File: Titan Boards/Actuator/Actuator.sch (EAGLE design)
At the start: 74 parts, among them Q1 MOSFET-NCH-AO3404A, Q12 MOSFET-NCH-AO3404A, Q13 MOSFET-NCH-AO3404A, Q14 MOSFET-NCH-AO3404A, Q15 MOSFET-NCH-AO3404A, Q17 MOSFET-NCH-AO3404A, Q18 FDD4141TO252, Q2 MOSFET-NCH-AO3404A, Q3 MOSFET-NCH-AO3404A, Q4 MOSFET-NCH-AO3404A, Q5 MOSFET-NCH-AO3404A, Q6 FDD4141TO252, Y1 12MHz, Y3 32.768kHz

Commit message: actuator board work TL
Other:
- note added: "WIP Notes: (I used my board as a start template because it had most of the microcontroller routing) - Moved capacitor to top right - Spaced out the torpedo parts a little - Made the microcontroller a bit more in center -TL 11/12: Routed bottom-left; dropper resistors Things still needed: - Labels positioned for LED's - Cleanup of all labels"
- note removed: "WIP Notes: (I used my board as a start template because it had most of the microcontroller routing) - Moved capacitor to top right - Spaced out the torpedo parts a little - Made the microcontroller a bit more in center Things still needed: - Labels positioned for LED's - Converter section (bottom left) (This is probably something good to take from your board) - Cleanup of all labels"
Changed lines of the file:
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@@
 - Spaced out the torpedo parts a little
 - Made the microcontroller a bit more in center
+-TL 11/12: Routed bottom-left; dropper resistors
 Things still needed:
 - Labels positioned for LED's
-- Converter section (bottom left)
-(This is probably something good to take
-from your board)
 - Cleanup of all labels</text>
 </plain>

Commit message: Titan Actuator Review Copy
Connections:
- net +3V3: now also U$1.SPARE7
- net EXTRA4: no longer U$1.SPARE7
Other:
- note removed: "WIP Notes: (I used my board as a start template because it had most of the microcontroller routing) - Moved capacitor to top right - Spaced out the torpedo parts a little - Made the microcontroller a bit more in center -TL 11/12: Routed bottom-left; dropper resistors Things still needed: - Labels positioned for LED's - Cleanup of all labels"
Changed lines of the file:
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@@
 <part name="AGND15" library="supply1" library_urn="urn:adsk.eagle:library:371" deviceset="AGND" device=""/>
 <part name="FRAME2" library="frames" library_urn="urn:adsk.eagle:library:229" deviceset="A3L-LOC" device=""/>
+<part name="+3V4" library="supply1" library_urn="urn:adsk.eagle:library:371" deviceset="+3V3" device=""/>
+<part name="+3V5" library="supply1" library_urn="urn:adsk.eagle:library:371" deviceset="+3V3" device=""/>
+<part name="+3V6" library="supply1" library_urn="urn:adsk.eagle:library:371" deviceset="+3V3" device=""/>
 </parts>
 <sheets>
@@
 <attribute name="VALUE" x="317.5" y="33.02" size="1.778" layer="96" rot="R180"/>
 </instance>
+<instance part="+3V4" gate="G$1" x="134.62" y="228.6" smashed="yes">
+<attribute name="VALUE" x="137.16" y="231.14" size="1.778" layer="96" rot="R180"/>
+</instance>
+<instance part="+3V5" gate="G$1" x="45.72" y="292.1" smashed="yes">
+<attribute name="VALUE" x="48.26" y="294.64" size="1.778" layer="96" rot="R180"/>
+</instance>
+<instance part="+3V6" gate="G$1" x="119.38" y="17.78" smashed="yes" rot="R180">
+<attribute name="VALUE" x="116.84" y="15.24" size="1.778" layer="96" rot="R90"/>
+</instance>
 </instances>
 <busses>
@@
 </segment>
 <segment>
-<wire x1="134.62" y1="231.14" x2="134.62" y2="210.82" width="0.1524" layer="91"/>
+<wire x1="134.62" y1="231.14" x2="134.62" y2="226.06" width="0.1524" layer="91"/>
+<wire x1="134.62" y1="226.06" x2="134.62" y2="210.82" width="0.1524" layer="91"/>
 <wire x1="134.62" y1="210.82" x2="129.54" y2="210.82" width="0.1524" layer="91"/>
 <pinref part="JTAG_HEADER" gate="G$1" pin="2"/>
@@
 <junction x="132.08" y="231.14"/>
 <pinref part="+3V2" gate="G$1" pin="+3V3"/>
+<pinref part="+3V4" gate="G$1" pin="+3V3"/>
+<junction x="134.62" y="226.06"/>
 </segment>
 <segment>
@@
 <pinref part="+3V15" gate="G$1" pin="+3V3"/>
 </segment>
+<segment>
+<pinref part="U$1" gate="G$1" pin="SPARE7"/>
+<pinref part="+3V6" gate="G$1" pin="+3V3"/>
+<wire x1="119.38" y1="26.67" x2="119.38" y2="20.32" width="0.1524" layer="91"/>
+</segment>
 </net>
 <net name="AGND" class="0">
@@
 <net name="EXTRA4" class="0">
 <segment>
-<wire x1="119.38" y1="26.67" x2="119.38" y2="22.86" width="0.1524" layer="91"/>
-<label x="119.38" y="22.86" size="1.778" layer="95" rot="R270" xref="yes"/>
-<pinref part="U$1" gate="G$1" pin="SPARE7"/>
-</segment>
-<segment>
 <pinref part="MC" gate="G$1" pin="PC10"/>
 <wire x1="322.58" y1="124.46" x2="325.12" y2="124.46" width="0.1524" layer="91"/>
@@
      · Switch
 </text>
-<text x="283.972" y="123.952" size="3.556" layer="91" align="top-left">WIP Notes:
-(I used my board as a start template
-because it had most of the microcontroller
-routing)
-- Moved capacitor to top right
-- Spaced out the torpedo parts a little
-- Made the microcontroller a bit more in center
--TL 11/12: Routed bottom-left; dropper resistors
-Things still needed:
-- Labels positioned for LED's
-- Cleanup of all labels</text>
 </plain>
 <instances>

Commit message: Start of board review change, Actuator
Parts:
- added C1, C12: 0.1uF, rcl:C-EUC0603
- added C10: 1uF, rcl:C-EUC0603
- added C11, C6: 0.5uF, rcl:C-EUC0603
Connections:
- net +12V: no longer D8.C, D9.C
- net +3V3: now also C1.1, C10.1, C11.1, C12.1, C6.1
- net +5V: now also D8.C, D9.C
- net AGND: now also C1.2, C10.2, C11.2, C12.2, C6.2, USB_ID/USB_DP/USB_DN.SHIELD; no longer MARKER_DROPPER.1, MARKER_DROPPER.3
- net DROPPER1: now also MARKER_DROPPER.1
- net DROPPER2: now also MARKER_DROPPER.3
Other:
- note added: "Back voltage changed to 5V from 12V"
- note added: "Capacitances varied for decoupling"
- note added: "Change to variable voltage"
- note added: "Increase transistor specs"
- note added: "Review Notes: Move capacitors/crystal oscillators closer to the micro controlller. Need decoupling capacitors on 3.3 Redo marker dropper connector Beefier transisitors for torpedo Microcontroller debug lights Variable voltage power supply"

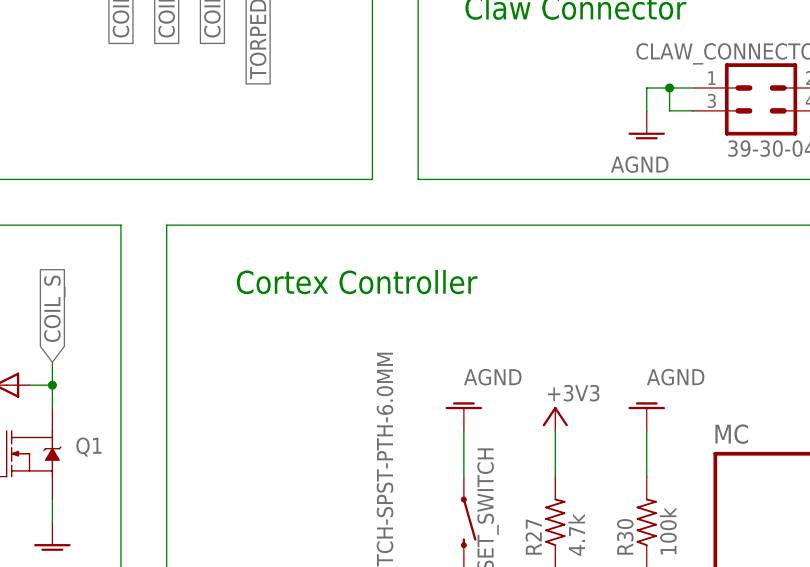
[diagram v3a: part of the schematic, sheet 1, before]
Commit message: name changes on microcontroller TL
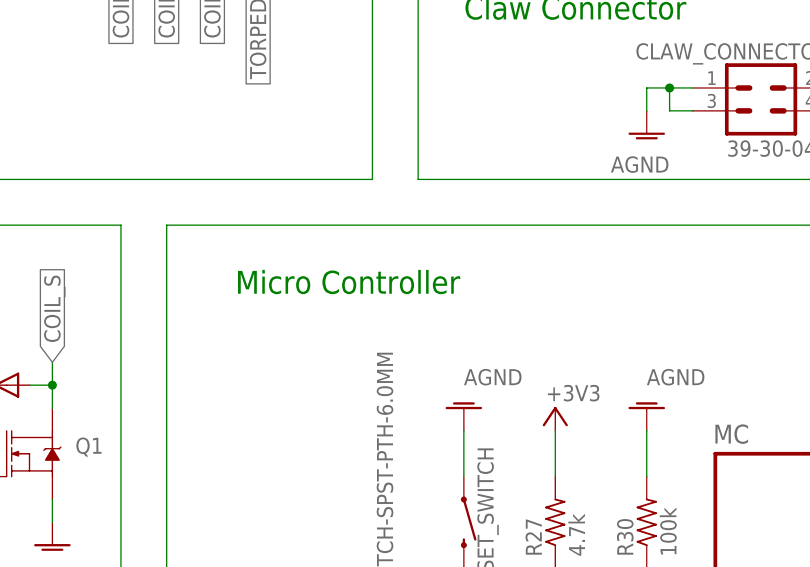
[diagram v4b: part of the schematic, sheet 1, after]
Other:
- note added: "Micro Controller"
- note removed: "Cortex Controller"
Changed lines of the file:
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@@
 <text x="238.76" y="246.38" size="2.54" layer="91">Marker Dropper</text>
 <text x="276.86" y="45.72" size="2.54" layer="91">Power Input</text>
-<text x="213.36" y="193.04" size="2.54" layer="91">Cortex Controller</text>
+<text x="213.36" y="193.04" size="2.54" layer="91">Micro Controller</text>
 <text x="154.94" y="127" size="1.778" layer="91">Back voltage changed to 5V from 12V</text>
 <text x="327.66" y="144.78" size="1.778" layer="91">Capacitances varied for decoupling</text>

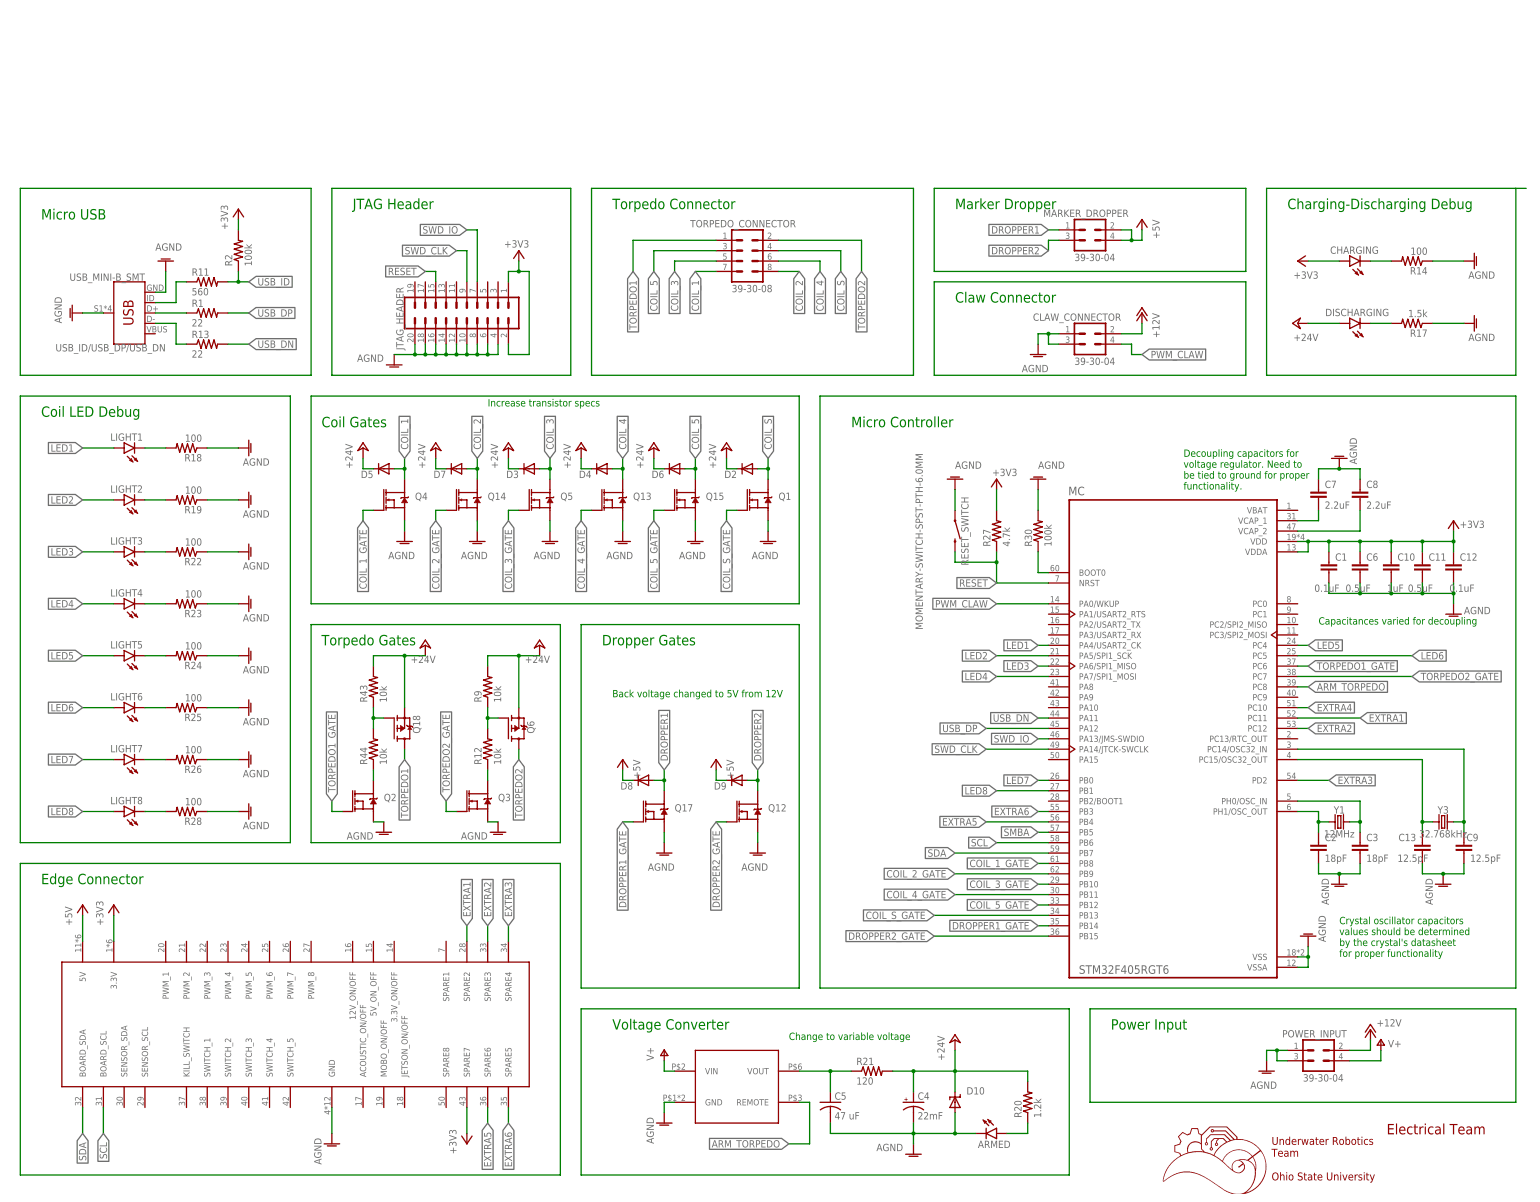
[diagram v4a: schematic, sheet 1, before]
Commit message: Actuator VBUS converter, crystal changes
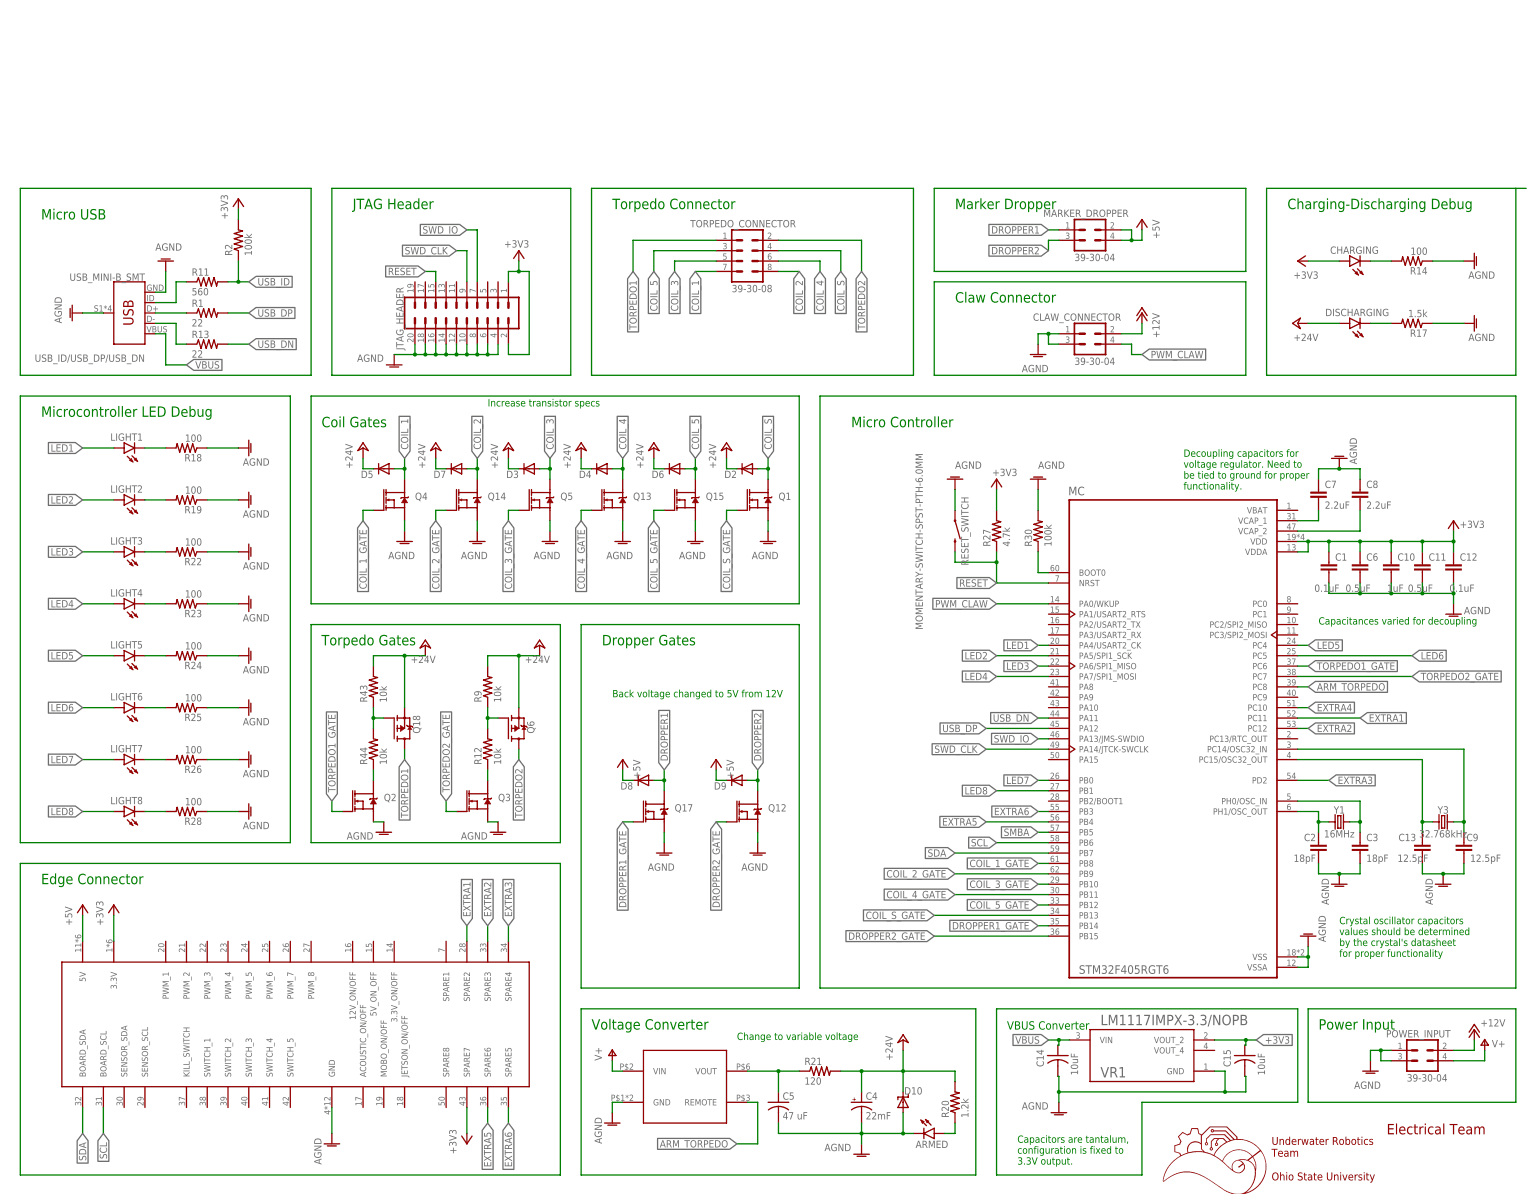
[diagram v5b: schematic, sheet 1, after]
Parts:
- added C14, C15: 10uF, rcl:C-USC0603
- added VR1: LM1117IMPX-3.3/NOPB, LM1117IMPX-3.3_NOPB:LM1117IMPX-3.3/NOPB
- Y1: value 12MHz -> 16MHz
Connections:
- new net VBUS: C14.1, USB_ID/USB_DP/USB_DN.VBUS, VR1.VIN
- net +3V3: now also C15.1, VR1.VOUT_2
- net AGND: now also C14.2, C15.2, VR1.GND
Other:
- note added: "Capacitors are tantalum, configuration is fixed to 3.3V output."
- note added: "Microcontroller LED Debug"
- note added: "Part Notes: JTAG Header: CONN_10X2 20 Position Header Connector Through Hole https://www.digikey.com/en/products/detail/sullins-connector-solutions/PPPC102LFBN-RC/807245 Board Connectors: 5530843-6 56 Position Female Connector Non Specified - Dual Edge Gold 0.100 in (2.54mm) Black https://www.digikey.com/product-detail/en/te-connectivity-amp-connectors/5530843-6/A31719-ND/770545 Torpedo Connector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"
- note added: "VBUS Converter"
- note removed: "Coil LED Debug"
- note removed: "Part Notes: JTAG Header: CONN_10X2 (Version 1) LINK TBD Board Connectors: 5530843-6 56 Position Female Connector Non Specified - Dual Edge Gold 0.100 in (2.54mm) Black https://www.digikey.com/product-detail/en/te-connectivity-amp-connectors/5530843-6/A31719-ND/770545 Torpedo Connector: 0039301080 Connector Header Through Hole, Right Angle 8 position 0.165" (4.20mm) con-molex minifit jr. https://w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"
- note removed: "Review Notes: Move capacitors/crystal oscillators closer to the micro controlller. Need decoupling capacitors on 3.3 Redo marker dropper connector Beefier transisitors for torpedo Microcontroller debug lights Variable voltage power supply"
- moved on the sheet: ARMED, C4, C5, D10, POWER_INPUT, R2, R20, R21
